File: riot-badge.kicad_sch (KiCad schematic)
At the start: 34 parts, among them J1 SAO, J2 UEXT, J3 SWD, J4 USB_C_Receptacle_USB2.0_16P, SW1 SW_Push, SW2 SW_Push, U1 XC6206PxxxMR

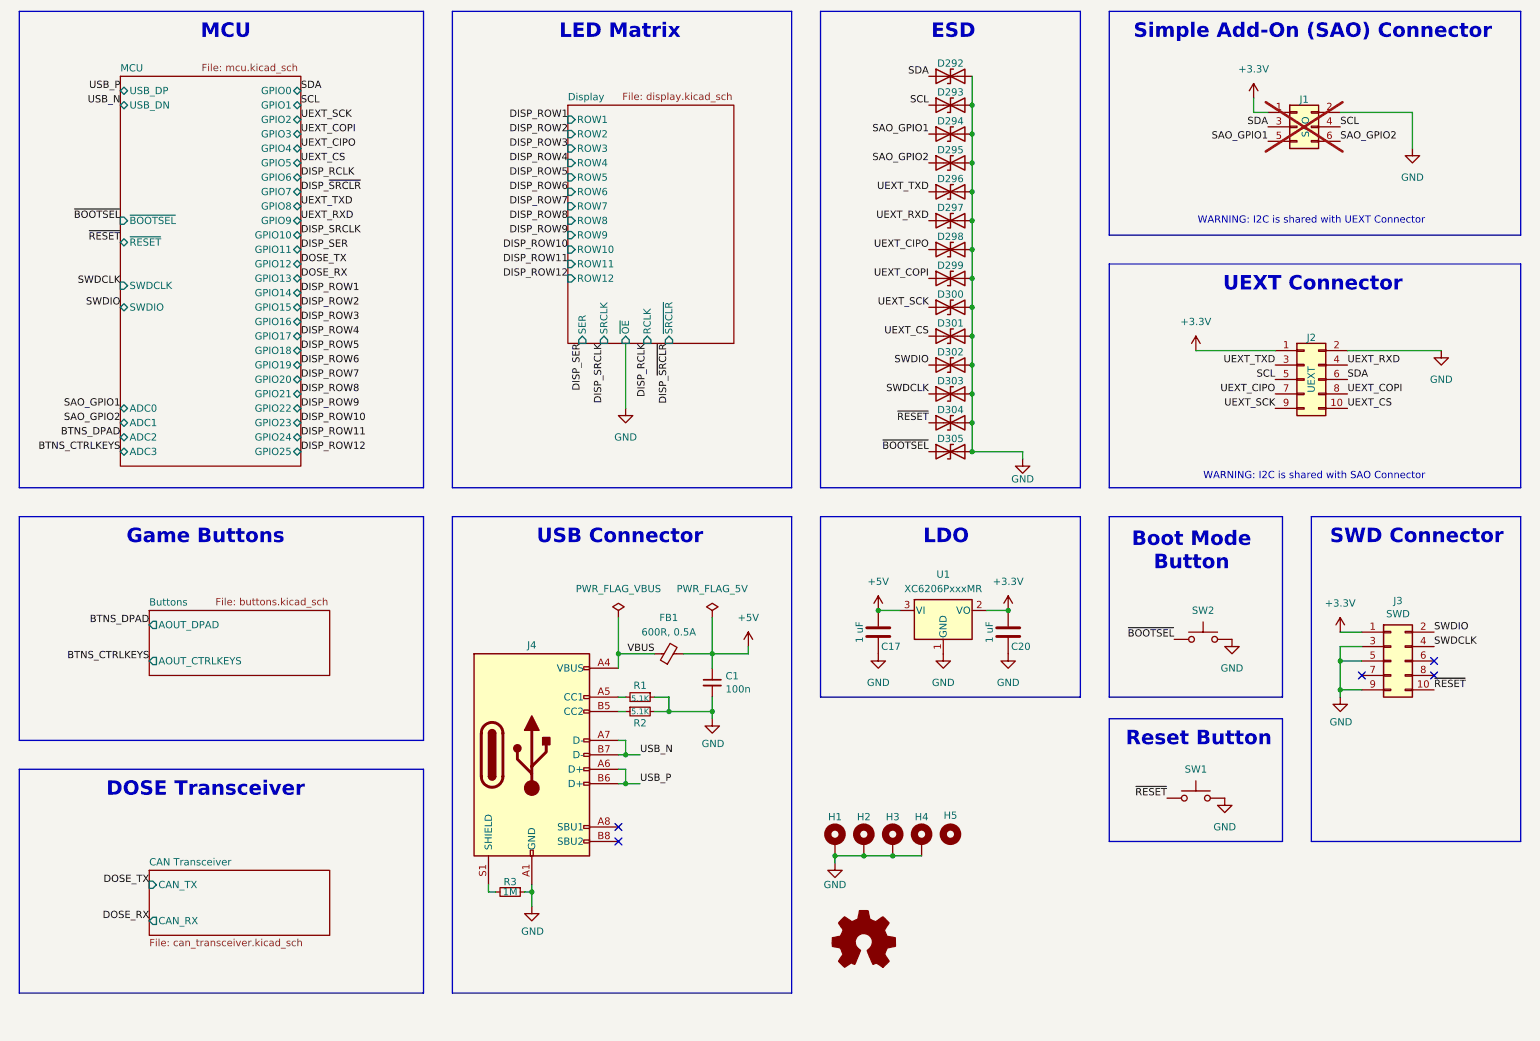
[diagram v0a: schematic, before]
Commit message: Updated badge based on feedback from badge.team
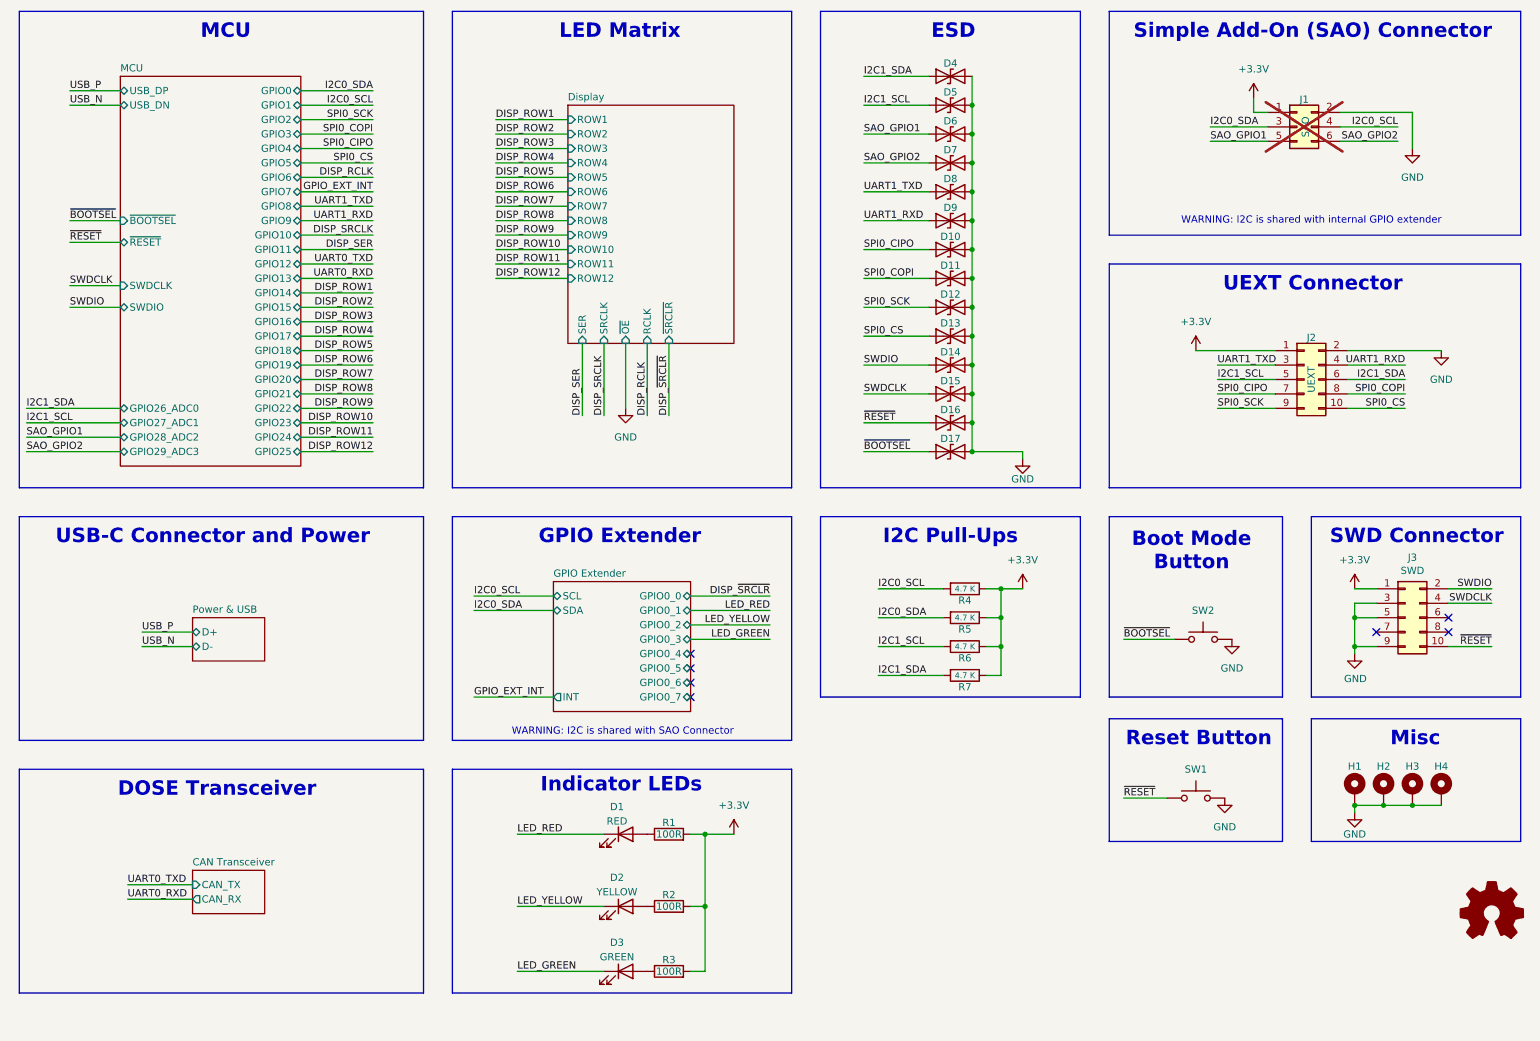
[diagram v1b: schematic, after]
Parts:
- removed C1: 100n, Capacitor_SMD:C_0402_1005Metric, symbol Device:C_Small
- removed C17, C20: 1 uF, Capacitor_SMD:C_0402_1005Metric, symbol Device:C
- removed D293, D294, D295, D296, D297, D298, D299, D300, D301, D302, D303, D304, D305: D_TVS, custom:DFN0603-2L-BI, symbol Device:D_TVS
- removed FB1: 600R, 0.5A, Inductor_SMD:L_0805_2012Metric, symbol Device:FerriteBead_Small
- removed H5: MountingHole, MountingHole:MountingHole_3mm, symbol Mechanical:MountingHole
- removed J4: USB_C_Receptacle_USB2.0_16P, Connector_USB:USB_C_Receptacle_GCT_USB4105-xx-A_16P_TopMnt_Horizontal, symbol Connector:USB_C_Receptacle_USB2.0_16P
- removed R1, R2: 5.1K, Resistor_SMD:R_0402_1005Metric, symbol Device:R_Small
- removed R3: 1M, Resistor_SMD:R_0402_1005Metric, symbol Device:R_Small
- removed U1: XC6206PxxxMR, Package_TO_SOT_SMD:SOT-23-3, symbol Regulator_Linear:XC6206PxxxMR
- added D1: RED, LED_SMD:LED_0603_1608Metric, symbol Device:LED
- added D10, D11, D12, D13, D14, D15, D16, D17, D5, D6, D7, D8, D9: D_TVS, custom:SOD-882_L1.0-W0.6-BI, symbol Device:D_TVS
- added D2: YELLOW, LED_SMD:LED_0805_2012Metric, symbol Device:LED
- added D3: GREEN, LED_SMD:LED_0805_2012Metric, symbol Device:LED
- added R1, R2, R3: 100R, Resistor_SMD:R_0402_1005Metric, symbol Device:R
- added R4, R5, R6, R7: 4.7 K, Resistor_SMD:R_0402_1005Metric, symbol Device:R
- D4: renamed from D292; footprint custom:DFN0603-2L-BI -> custom:SOD-882_L1.0-W0.6-BI; LCSC (none) -> C7420372
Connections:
- net +3.3V: now also R1.2, R2.2, R3.2, R4.1, R5.1, R6.1, R7.1
- net GND: now also D10.2 (A2), D11.2 (A2), D12.2 (A2), D13.2 (A2), D14.2 (A2), D15.2 (A2), D16.2 (A2), D17.2 (A2), D5.2 (A2), D6.2 (A2), D7.2 (A2), D8.2 (A2), D9.2 (A2)
- net SAO_GPIO1: now also D6.1 (A1)
- net SAO_GPIO2: now also D7.1 (A1)
- net SWDCLK: now also D15.1 (A1)
- net SWDIO: now also D14.1 (A1)
- net ~{BOOTSEL}: now also D17.1 (A1)
- net ~{RESET}: now also D16.1 (A1)
- net SCL renamed I2C0_SCL
- net I2C0_SCL: now also R4.2; no longer J2.5 (Pin_5)
- net SDA renamed I2C1_SDA
- net I2C1_SDA: now also R7.2; no longer J1.3 (Pin_3)
- net UEXT_CIPO renamed SPI0_CIPO
- net SPI0_CIPO: now also D10.1 (A1)
- net UEXT_COPI renamed SPI0_COPI
- net SPI0_COPI: now also D11.1 (A1)
- net UEXT_CS renamed SPI0_CS
- net SPI0_CS: now also D13.1 (A1)
- net UEXT_RXD renamed UART1_RXD
- net UART1_RXD: now also D9.1 (A1)
- net UEXT_SCK renamed SPI0_SCK
- net SPI0_SCK: now also D12.1 (A1)
- net UEXT_TXD renamed UART1_TXD
- net UART1_TXD: now also D8.1 (A1)
- new net: D3.2 (A), R3.1
- new net: D2.2 (A), R2.1
- new net: D1.2 (A), R1.1
- new net I2C0_SDA: J1.3 (Pin_3), R5.2
- new net I2C1_SCL: D5.1 (A1), J2.5 (Pin_5), R6.2
- new net LED_GREEN: D3.1 (K)
- new net LED_RED: D1.1 (K)
- new net LED_YELLOW: D2.1 (K)
- no-connect marks 5 -> 7
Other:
- sheet Buttons renamed GPIO Extender
- added sheet Power & USB (power_usb.kicad_sch)
- sheet GPIO Extender: file buttons.kicad_sch -> gpio_extender.kicad_sch
- sheet GPIO Extender ports: added GPIO0_0, GPIO0_1, GPIO0_2, GPIO0_3, GPIO0_4, GPIO0_5, GPIO0_6, GPIO0_7, INT, SCL, SDA; removed AOUT_CTRLKEYS, AOUT_DPAD
- sheet MCU ports: added GPIO26_ADC0, GPIO27_ADC1, GPIO28_ADC2, GPIO29_ADC3; removed ADC0, ADC1, ADC2, ADC3
- note added: "GPIO Extender"
- note added: "I2C Pull-Ups"
- note added: "Indicator LEDs"
- note added: "Misc"
- note added: "USB-C Connector and Power"
- note added: "WARNING: I2C is shared with internal GPIO extender"
- note removed: "Game Buttons"
- note removed: "LDO"
- note removed: "USB Connector"
- note removed: "WARNING: I2C is shared with UEXT Connector"
- company: (none) -> Marian Buschsieweke
- title: (none) -> Badge for RIOT Summit '25
- moved on the sheet: H1, H2, H3, H4, J3

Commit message: Schematics: Add uSD card holder & VBAT sensing
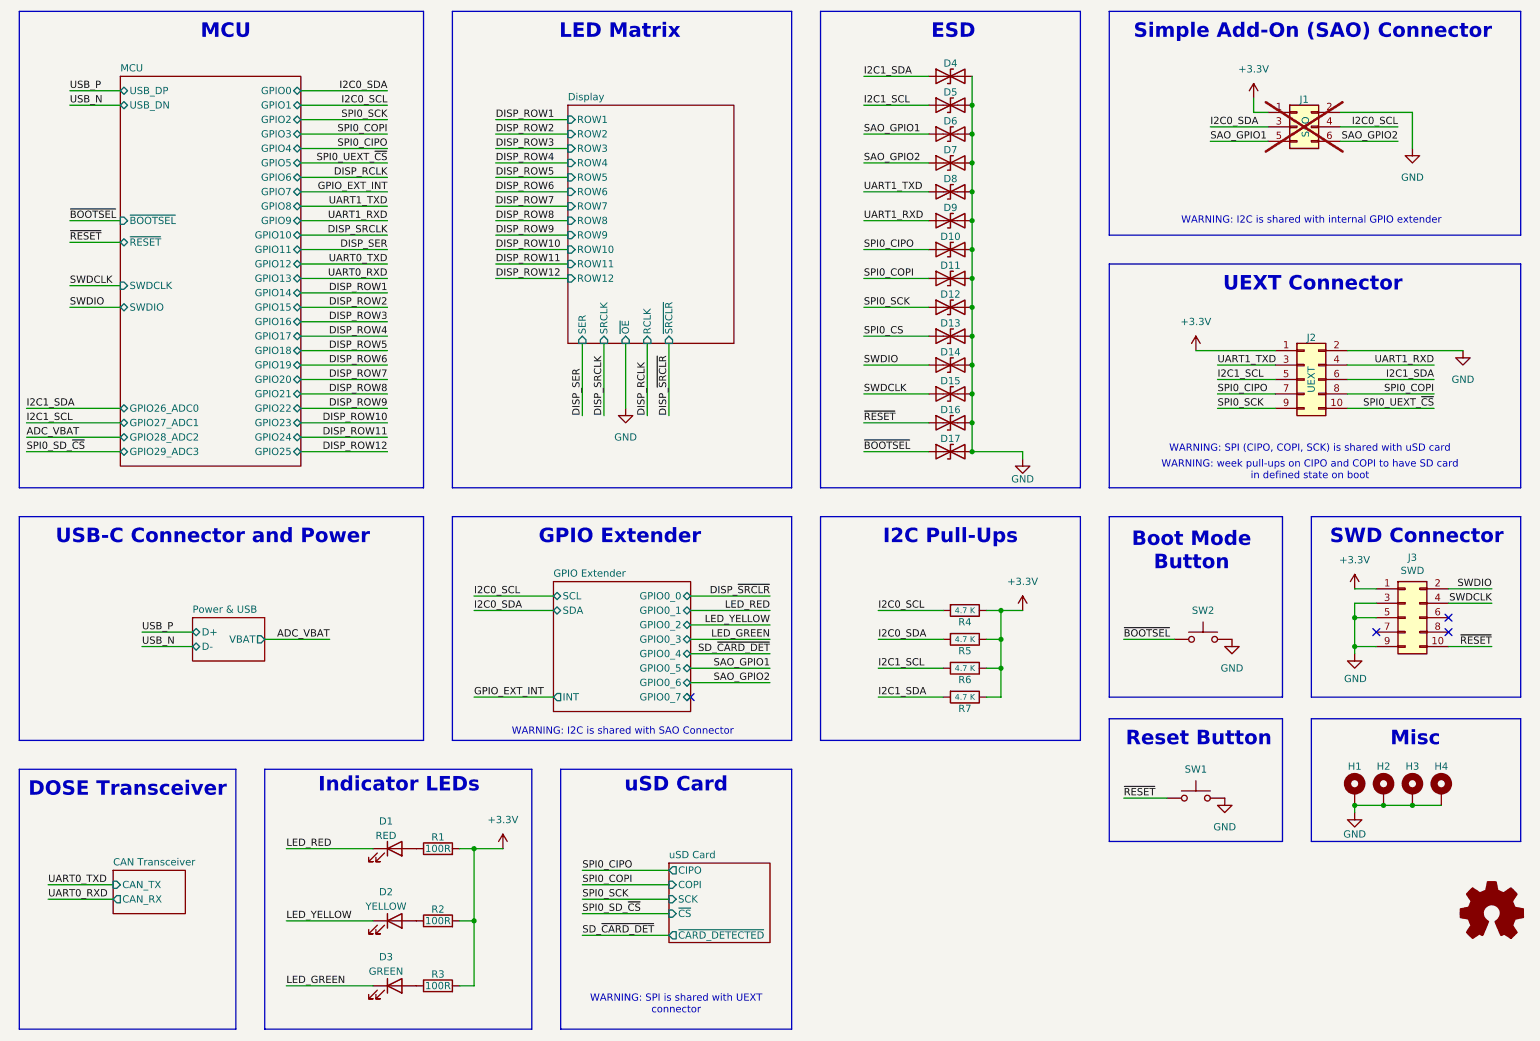
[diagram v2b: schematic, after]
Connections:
- net SPI0_CS: no longer J2.10 (Pin_10)
- new net SPI0_UEXT_~{CS}: J2.10 (Pin_10)
- no-connect marks 7 -> 4
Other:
- added sheet uSD Card (sd_card.kicad_sch)
- sheet Power & USB ports: added VBAT; removed none
- note added: "WARNING: SPI (CIPO, COPI, SCK) is shared with uSD card"
- note added: "WARNING: SPI is shared with UEXT connector"
- note added: "WARNING: week pull-ups on CIPO and COPI to have SD card in defined state on boot"
- note added: "uSD Card"
- moved on the sheet: D1, D2, D3, R1, R2, R3, R4, R5, R6, R7

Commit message: Schematics: Add accelerometer, drop VBAT sensing
Adding a cheap accelerometer to the boards, sacraficing the VBAT input
to make room for the /CS pin.
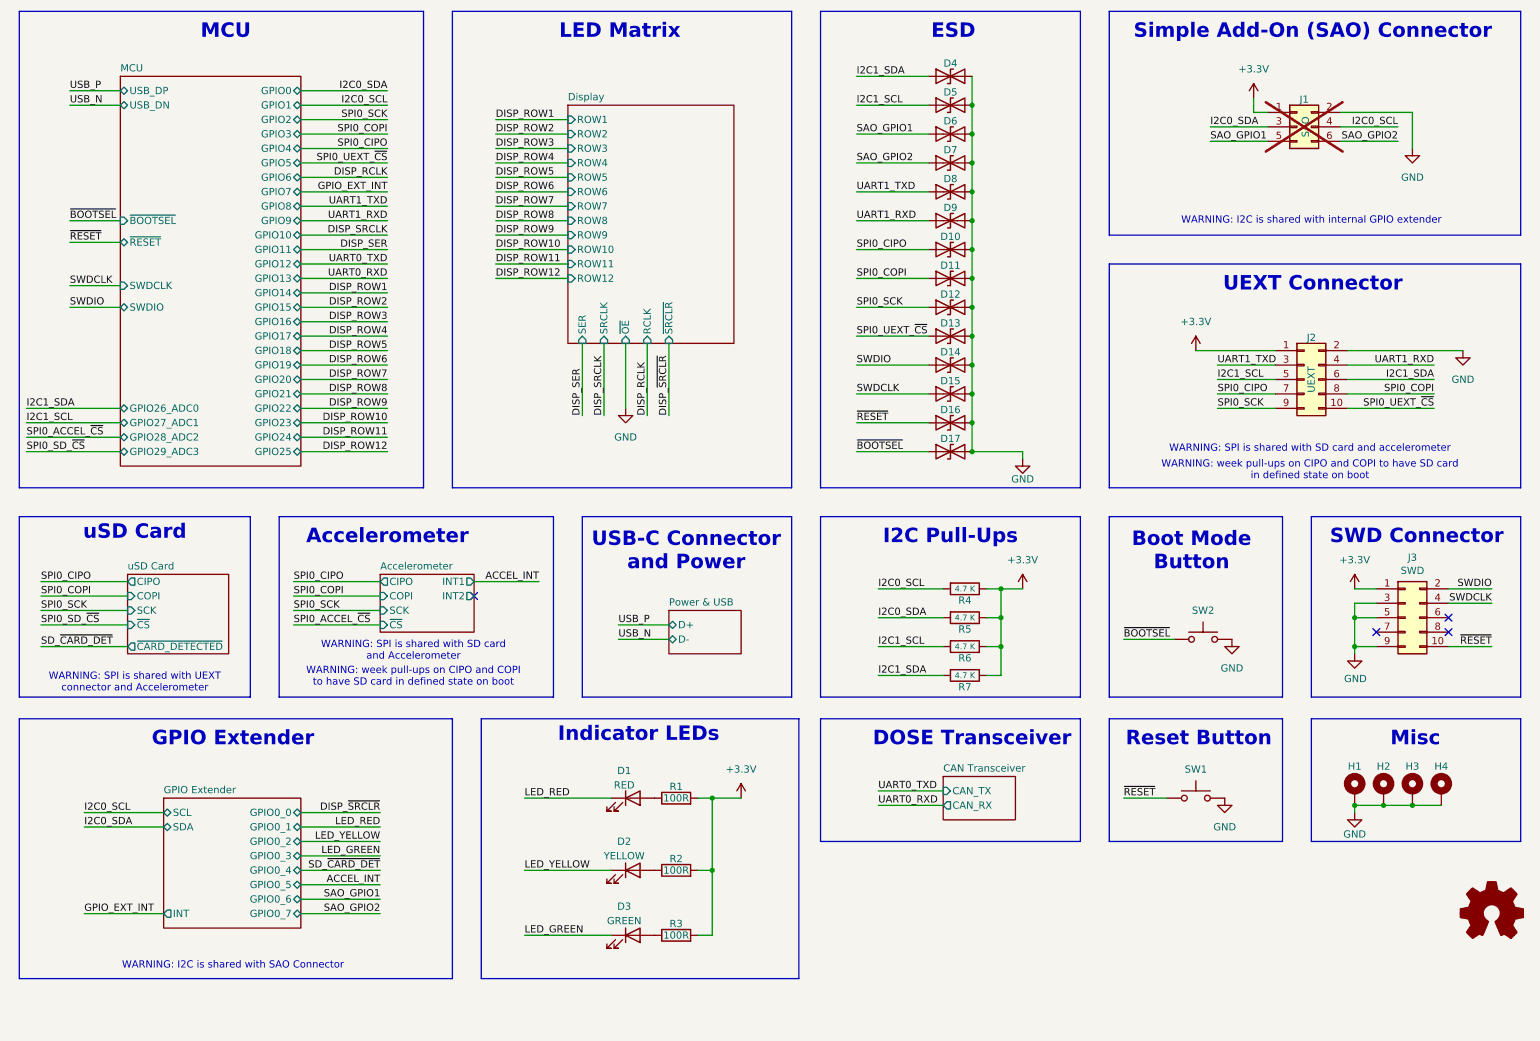
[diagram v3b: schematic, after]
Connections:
- net SPI0_CS is gone; now on net SPI0_UEXT_~{CS}: D13.1 (A1)
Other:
- added sheet Accelerometer (accelerometer.kicad_sch)
- sheet Power & USB ports: added none; removed VBAT
- note added: "Accelerometer"
- note added: "WARNING: SPI is shared with SD card and Accelerometer"
- note added: "WARNING: SPI is shared with SD card and accelerometer"
- note added: "WARNING: SPI is shared with UEXT connector and Accelerometer"
- note removed: "WARNING: SPI (CIPO, COPI, SCK) is shared with uSD card"
- note removed: "WARNING: SPI is shared with UEXT connector"
- moved on the sheet: D1, D2, D3, R1, R2, R3, R4, R5, R6, R7
